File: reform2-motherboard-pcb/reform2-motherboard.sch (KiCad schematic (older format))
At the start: 46 parts, among them J15 Conn_01x33, J18 Conn_01x03_Male, J19 JTAG, J20 Conn_01x03_Male, SW3 SW_DIP_x01, SW5 SW_DIP_x04, SW6 SW_Push, U1 Nitrogen8M

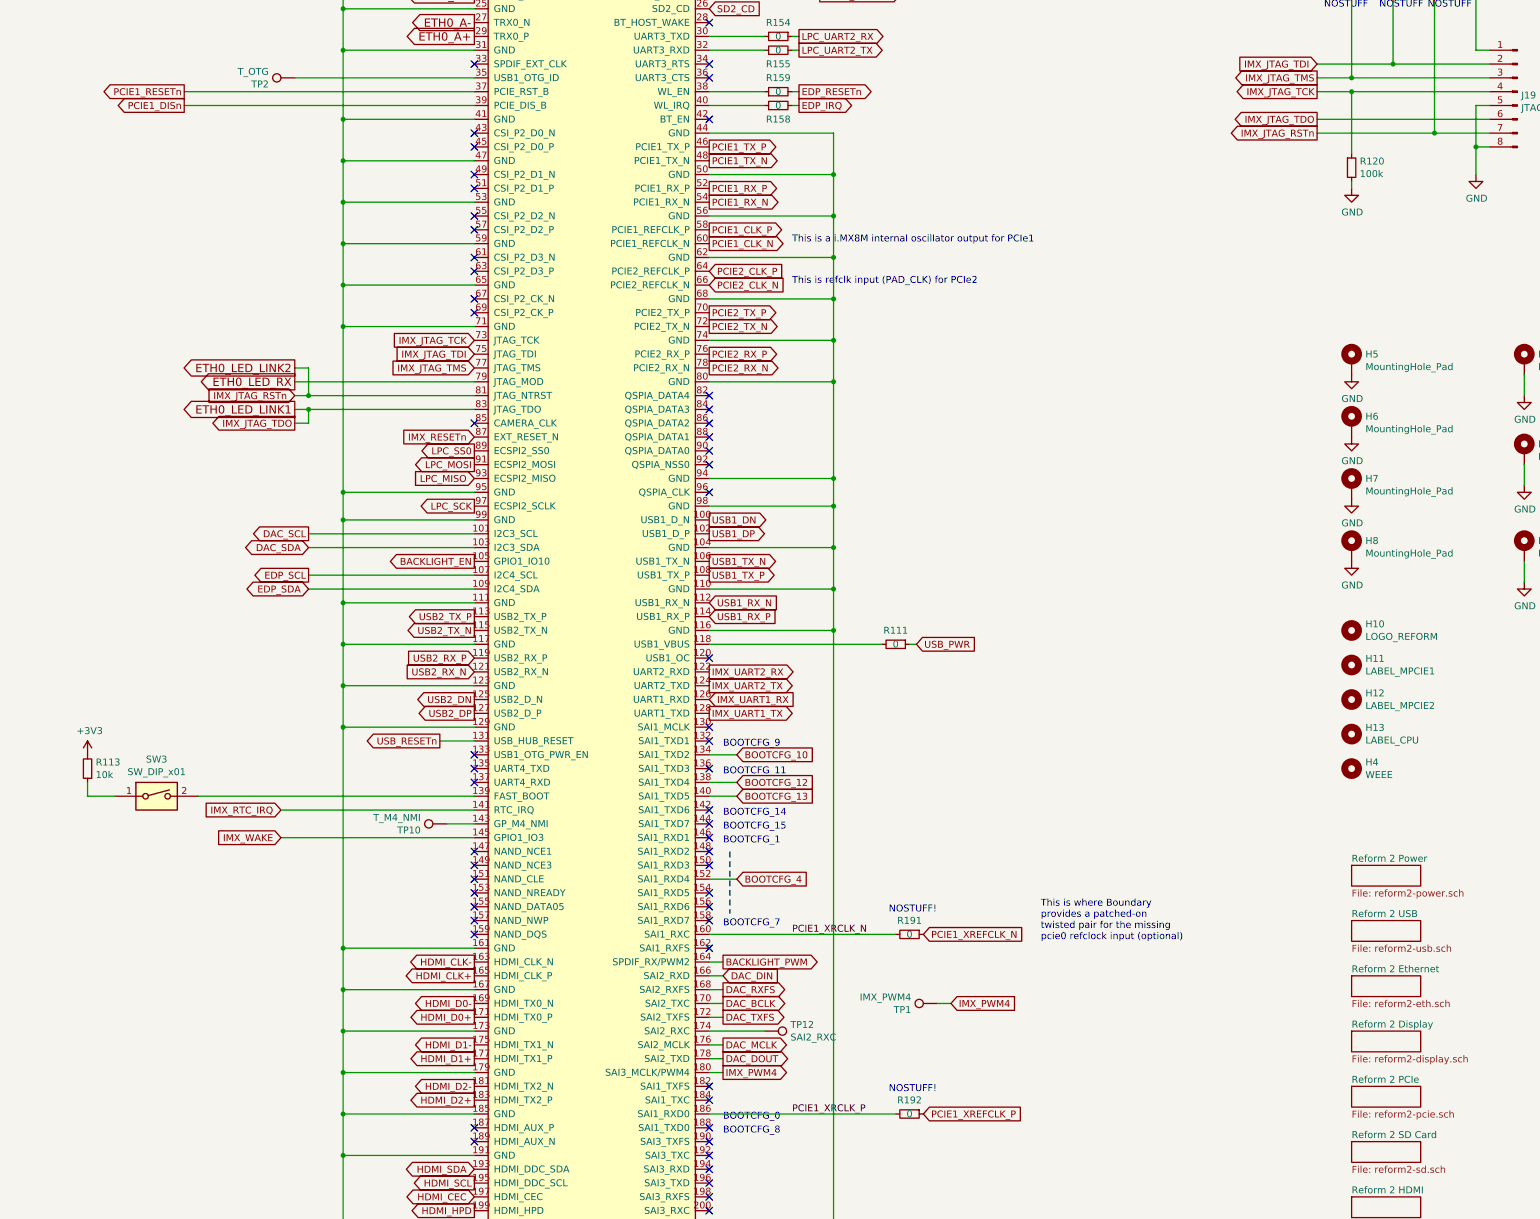
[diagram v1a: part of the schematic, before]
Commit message: reform2-motherboard: version D-4 finished; fixes critical D-3 bugs; adds PCIe refclk termination, speaker output filter stage, pcie0 3v3 load switch, imx reset line to lpc, charge current control line to lpc
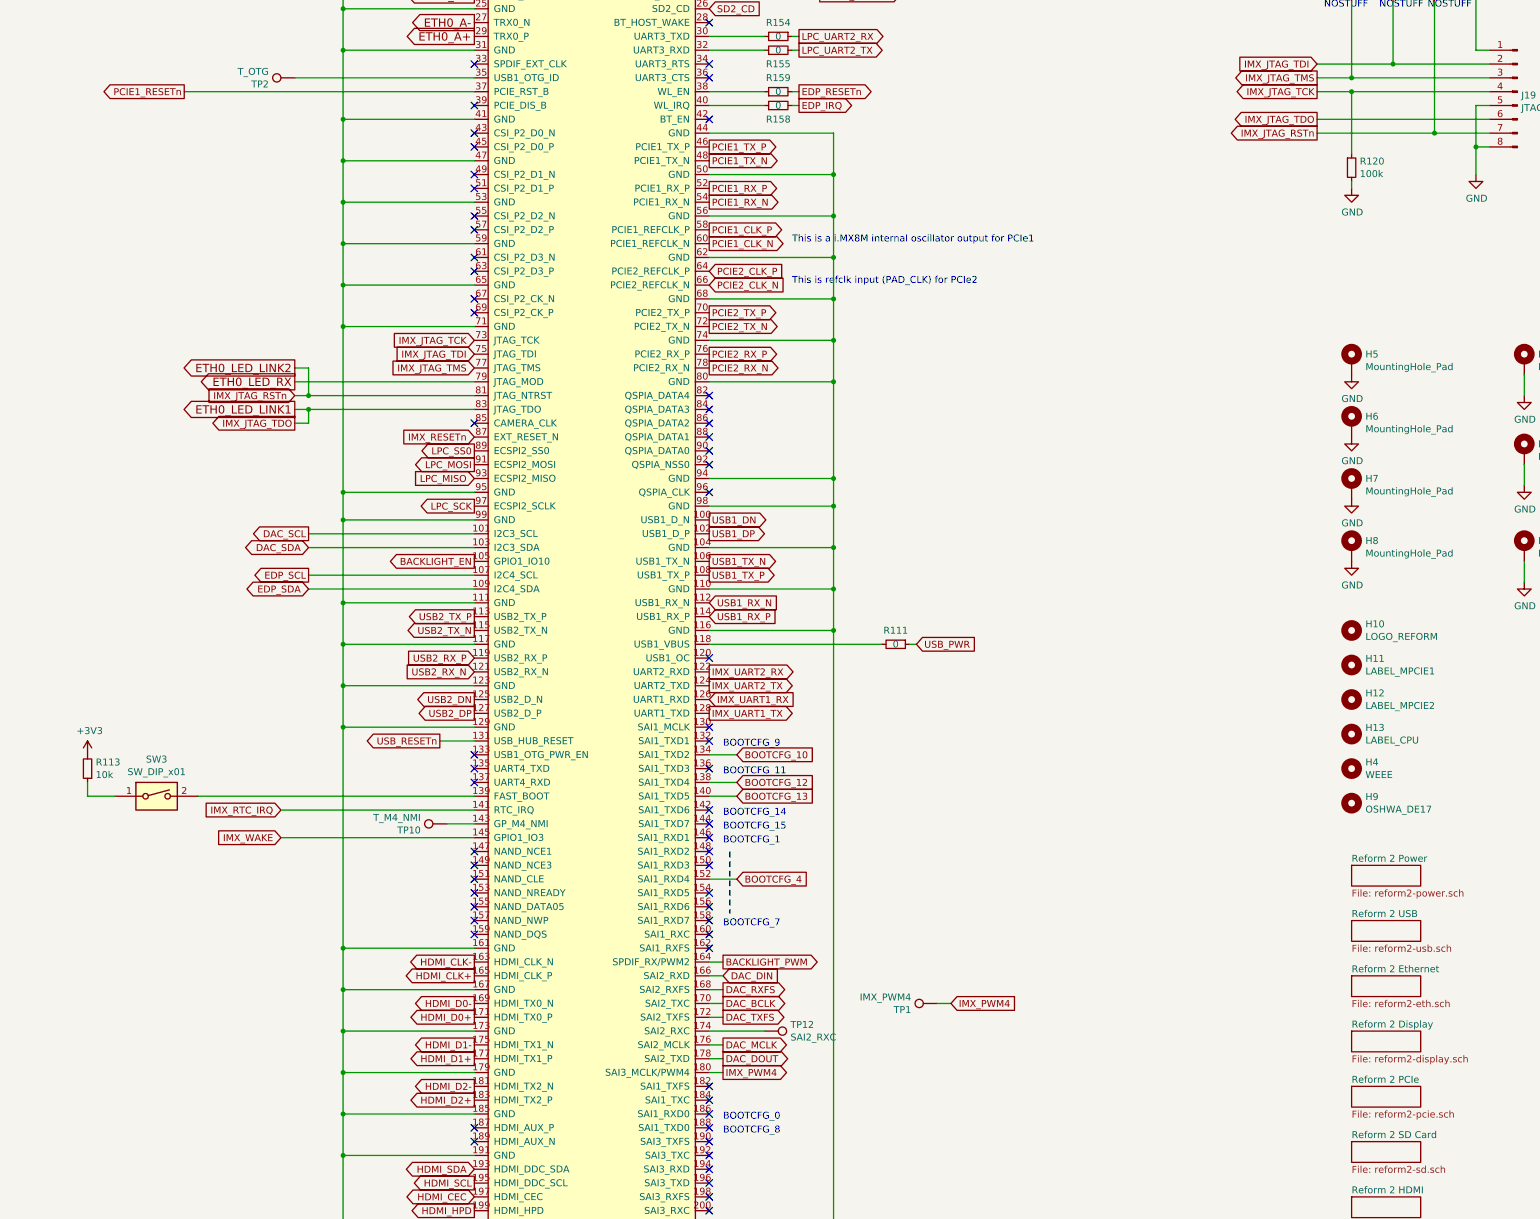
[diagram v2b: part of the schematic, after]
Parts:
- removed R191, R192: 0, Resistor_SMD:R_0603_1608Metric, symbol Device:R_Small
- added H9: OSHWA_DE17, footprints:oshwa-de17, symbol Mechanical:MountingHole
- H1, H10, H11, H12, H13, H2, H3, H4, H5, H6, H7, H8, R117, R118, R119, TP1, TP10, TP12, TP2, TP8: DNP (none) -> y
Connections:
- net PCIE1_DISn: no longer names the net of U1.39 (PCIE_DIS_B)
- net PCIE1_XRCLK_N: no longer names the net of U1.160 (SAI1_RXC)
- net PCIE1_XRCLK_P: no longer names the net of U1.186 (SAI1_RXD0)
- no-connect marks 72 -> 75
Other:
- note removed: "NOSTUFF!"
- note removed: "This is where Boundary\nprovides a patched-on\ntwisted pair for the missing\npcie0 refclock input (optional)\n"
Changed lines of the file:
@@
 Sheet 1 9
 Title "MNT Reform 2"
-Date "2020-04-11"
+Date "2020-05-19"
 Rev "2.0D-4"
 Comp "MNT Research GmbH"
@@
 F 4 "y" H 7400 5250 50  0001 C CNN "Checked"
 F 5 "None" H 7400 5250 50  0001 C CNN "Distributor"
+F 6 "y" H 7400 5250 50  0001 C CNN "DNP"
 	1    7400 5250
 	0    -1   -1   0
@@
 F 4 "y" H 15050 10000 50  0001 C CNN "Checked"
 F 5 "None" H 15050 10000 50  0001 C CNN "Distributor"
+F 6 "y" H 15050 10000 50  0001 C CNN "DNP"
 	1    15050 10000
 	1    0    0    -1
@@
 F 4 "y" H 11800 3850 50  0001 C CNN "Checked"
 F 5 "None" H 11800 3850 50  0001 C CNN "Distributor"
+F 6 "y" H 11800 3850 50  0001 C CNN "DNP"
 	1    11800 3850
 	0    1    1    0
@@
 F 4 "y" H 16300 8650 50  0001 C CNN "Checked"
 F 5 "None" H 16300 8650 50  0001 C CNN "Distributor"
+F 6 "y" H 16300 8650 50  0001 C CNN "DNP"
 	1    16300 8650
 	1    0    0    -1
@@
 F 4 "y" H 16300 7950 50  0001 C CNN "Checked"
 F 5 "None" H 16300 7950 50  0001 C CNN "Distributor"
+F 6 "y" H 16300 7950 50  0001 C CNN "DNP"
 	1    16300 7950
 	1    0    0    -1
@@
 F 4 "y" H 16300 7300 50  0001 C CNN "Checked"
 F 5 "None" H 16300 7300 50  0001 C CNN "Distributor"
+F 6 "y" H 16300 7300 50  0001 C CNN "DNP"
 	1    16300 7300
 	1    0    0    -1
@@
 F 6 "y" H 15650 4600 50  0001 C CNN "Checked"
 F 7 "Mouser" H 15650 4600 50  0001 C CNN "Distributor"
+F 8 "y" H 15650 4600 50  0001 C CNN "DNP"
 	1    15650 4600
 	1    0    0    -1
@@
 F 6 "y" H 15350 4600 50  0001 C CNN "Checked"
 F 7 "Mouser" H 15350 4600 50  0001 C CNN "Distributor"
+F 8 "y" H 15350 4600 50  0001 C CNN "DNP"
 	1    15350 4600
 	1    0    0    -1
@@
 F 6 "y" H 15050 4600 50  0001 C CNN "Checked"
 F 7 "Mouser" H 15050 4600 50  0001 C CNN "Distributor"
+F 8 "y" H 15050 4600 50  0001 C CNN "DNP"
 	1    15050 4600
 	1    0    0    -1
@@
 F 4 "y" H 15050 8650 50  0001 C CNN "Checked"
 F 5 "None" H 15050 8650 50  0001 C CNN "Distributor"
+F 6 "y" H 15050 8650 50  0001 C CNN "DNP"
 	1    15050 8650
 	1    0    0    -1
@@
 F 4 "y" H 15050 8200 50  0001 C CNN "Checked"
 F 5 "None" H 15050 8200 50  0001 C CNN "Distributor"
+F 6 "y" H 15050 8200 50  0001 C CNN "DNP"
 	1    15050 8200
 	1    0    0    -1
@@
 F 4 "y" H 15050 7750 50  0001 C CNN "Checked"
 F 5 "None" H 15050 7750 50  0001 C CNN "Distributor"
+F 6 "y" H 15050 7750 50  0001 C CNN "DNP"
 	1    15050 7750
 	1    0    0    -1
@@
 F 4 "y" H 15050 7300 50  0001 C CNN "Checked"
 F 5 "None" H 15050 7300 50  0001 C CNN "Distributor"
+F 6 "y" H 15050 7300 50  0001 C CNN "DNP"
 	1    15050 7300
 	1    0    0    -1
@@
 F 4 "y" H 15050 9750 50  0001 C CNN "Checked"
 F 5 "None" H 15050 9750 50  0001 C CNN "Distributor"
+F 6 "y" H 15050 9750 50  0001 C CNN "DNP"
 	1    15050 9750
 	1    0    0    -1
@@
 F 4 "y" H 15050 9500 50  0001 C CNN "Checked"
 F 5 "None" H 15050 9500 50  0001 C CNN "Distributor"
+F 6 "y" H 15050 9500 50  0001 C CNN "DNP"
 	1    15050 9500
 	1    0    0    -1
@@
 F 4 "y" H 15050 9250 50  0001 C CNN "Checked"
 F 5 "None" H 15050 9250 50  0001 C CNN "Distributor"
+F 6 "y" H 15050 9250 50  0001 C CNN "DNP"
 	1    15050 9250
 	1    0    0    -1
@@
 F 4 "y" H 15050 10250 50  0001 C CNN "Checked"
 F 5 "None" H 15050 10250 50  0001 C CNN "Distributor"
+F 6 "y" H 15050 10250 50  0001 C CNN "DNP"
 	1    15050 10250
 	1    0    0    -1
@@
 F 4 "y" H 8500 10650 50  0001 C CNN "Checked"
 F 5 "None" H 8500 10650 50  0001 C CNN "Distributor"
+F 6 "y" H 8500 10650 50  0001 C CNN "DNP"
 	1    8500 10650
 	0    -1   -1   0
@@
 F 4 "y" H 10800 12150 50  0001 C CNN "Checked"
 F 5 "None" H 10800 12150 50  0001 C CNN "Distributor"
+F 6 "y" H 10800 12150 50  0001 C CNN "DNP"
 	1    10800 12150
 	0    1    1    0
@@
 Wire Wire Line
 	8700 10550 7300 10550
-Text GLabel 11950 12750 2    50   Input ~ 0
-PCIE1_XREFCLK_P
-Text GLabel 11950 11450 2    50   Input ~ 0
-PCIE1_XREFCLK_N
-Wire Wire Line
-	10400 12750 11750 12750
-Wire Wire Line
-	10400 11450 11750 11450
-$Comp
-L Device:R_Small R191
-U 1 1 5E410610
-P 11850 11450
-F 0 "R191" V 11750 11450 50  0000 C CNN
-F 1 "0" V 11850 11450 50  0000 C CNN
-F 2 "Resistor_SMD:R_0603_1608Metric" H 11850 11450 50  0001 C CNN
-F 3 "~" H 11850 11450 50  0001 C CNN
-F 4 "Vishay Dale" H 11850 11450 50  0001 C CNN "Manufacturer"
-F 5 "CRCW06030000Z0EAC" H 11850 11450 50  0001 C CNN "Manufacturer_No"
-F 6 "Mouser" H 11850 11450 50  0001 C CNN "Distributor"
-F 7 "y" H 11850 11450 50  0001 C CNN "Checked"
-	1    11850 11450
-	0    1    1    0
-$EndComp
-$Comp
-L Device:R_Small R192
-U 1 1 5E410B4B
-P 11850 12750
-F 0 "R192" V 11750 12750 50  0000 C CNN
-F 1 "0" V 11850 12750 50  0000 C CNN
-F 2 "Resistor_SMD:R_0603_1608Metric" H 11850 12750 50  0001 C CNN
-F 3 "~" H 11850 12750 50  0001 C CNN
-F 4 "Vishay Dale" H 11850 12750 50  0001 C CNN "Manufacturer"
-F 5 "CRCW06030000Z0EAC" H 11850 12750 50  0001 C CNN "Manufacturer_No"
-F 6 "Mouser" H 11850 12750 50  0001 C CNN "Distributor"
-F 7 "y" H 11850 12750 50  0001 C CNN "Checked"
-	1    11850 12750
-	0    1    1    0
-$EndComp
-Text Notes 12800 11500 0    50   ~ 0
-This is where Boundary\nprovides a patched-on\ntwisted pair for the missing\npcie0 refclock input (optional)\n
-Text GLabel 6600 5450 0    50   Output ~ 0
-PCIE1_DISn
-Wire Wire Line
-	8700 5450 6600 5450
 Wire Wire Line
 	18200 3250 18300 3250
@@
 Wire Wire Line
 	18300 3250 18750 3250
-Text Label 11000 11450 0    50   ~ 0
-PCIE1_XRCLK_N
-Text Label 11000 12750 0    50   ~ 0
-PCIE1_XRCLK_P
 Wire Wire Line
 	6600 5350 8700 5350
 Wire Wire Line
 	10400 4650 11200 4650
-Text Notes 11700 11300 0    50   ~ 0
-NOSTUFF!
-Text Notes 11700 12600 0    50   ~ 0
-NOSTUFF!
 Wire Wire Line
 	10500 12450 10400 12450
@@
 F 4 "y" H 12050 11950 50  0001 C CNN "Checked"
 F 5 "None" H 12050 11950 50  0001 C CNN "Distributor"
+F 6 "y" H 12050 11950 50  0001 C CNN "DNP"
 	1    12050 11950
 	0    -1   -1   0
@@
 Wire Wire Line
 	7500 8850 8700 8850
+NoConn ~ 10400 11450
+NoConn ~ 10400 12750
+$Comp
+L Mechanical:MountingHole H9
+U 1 1 5EC23958
+P 15050 10500
+F 0 "H9" H 15150 10546 50  0000 L CNN
+F 1 "OSHWA_DE17" H 15150 10455 50  0000 L CNN
+F 2 "footprints:oshwa-de17" H 15050 10500 50  0001 C CNN
+F 3 "~" H 15050 10500 50  0001 C CNN
+F 4 "y" H 15050 10500 50  0001 C CNN "Checked"
+F 5 "None" H 15050 10500 50  0001 C CNN "Distributor"
+F 6 "y" H 15050 10500 50  0001 C CNN "DNP"
+	1    15050 10500
+	1    0    0    -1
+$EndComp
+NoConn ~ 8700 5450
 $EndSCHEMATC

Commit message: reform2-motherboard 2d4 component cleanup
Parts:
- SW3: Manufacturer Omron -> Apem; Manufacturer_No A6S-1101-H -> DM01
- SW6: Manufacturer CK -> C&K; Manufacturer_No KMR223NGULCLFG -> KMR221GLFS
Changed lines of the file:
@@
 F 2 "Button_Switch_SMD:SW_DIP_SPSTx01_Slide_Omron_A6S-110x_W8.9mm_P2.54mm" H 6400 10450 50  0001 C CNN
 F 3 "~" H 6400 10450 50  0001 C CNN
-F 4 "Omron" H 6400 10450 50  0001 C CNN "Manufacturer"
-F 5 "A6S-1101-H" H 6400 10450 50  0001 C CNN "Manufacturer_No"
+F 4 "Apem" H 6400 10450 50  0001 C CNN "Manufacturer"
+F 5 "DM01" H 6400 10450 50  0001 C CNN "Manufacturer_No"
 F 6 "y" H 6400 10450 50  0001 C CNN "Checked"
 F 7 "Mouser" H 6400 10450 50  0001 C CNN "Distributor"
@@
 F 2 "Button_Switch_SMD:SW_Push_1P1T_NO_CK_KMR2" H 18000 3450 50  0001 C CNN
 F 3 "~" H 18000 3450 50  0001 C CNN
-F 4 "CK" H 18000 3250 50  0001 C CNN "Manufacturer"
-F 5 "KMR223NGULCLFG" H 18000 3250 50  0001 C CNN "Manufacturer_No"
+F 4 "C&K" H 18000 3250 50  0001 C CNN "Manufacturer"
+F 5 "KMR221GLFS" H 18000 3250 50  0001 C CNN "Manufacturer_No"
 F 6 "y" H 18000 3250 50  0001 C CNN "Checked"
 F 7 "Mouser" H 18000 3250 50  0001 C CNN "Distributor"
